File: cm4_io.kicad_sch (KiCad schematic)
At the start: 6 parts, among them CN13 1-2301994-2

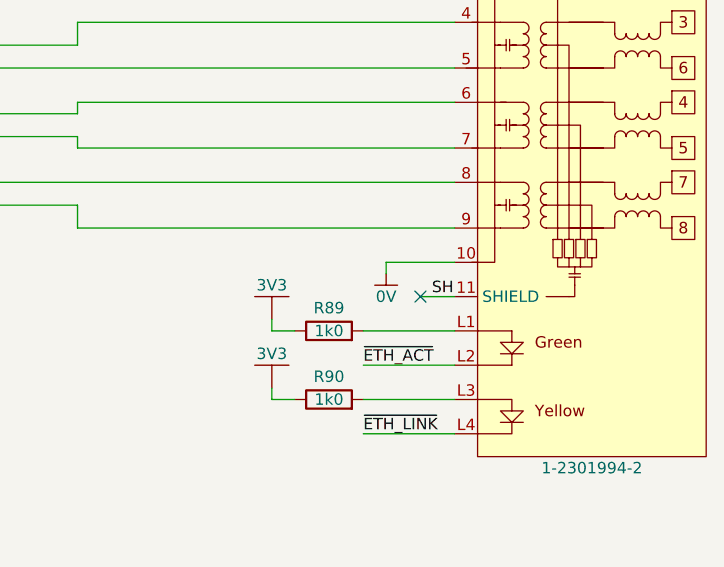
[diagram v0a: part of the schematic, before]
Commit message: Fixed connector offsets
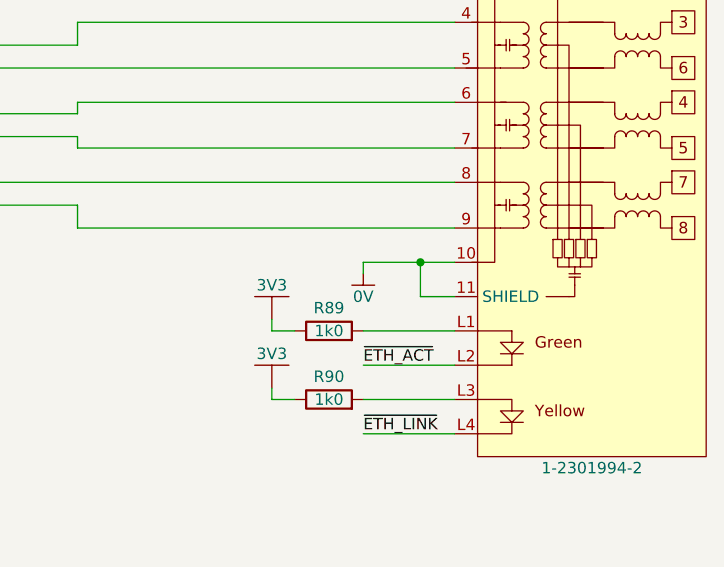
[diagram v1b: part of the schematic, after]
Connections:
- net SH is gone; now on net 0V: CN13.11 (SHIELD)
- no-connect marks 15 -> 14
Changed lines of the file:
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@@
   (junction (at 163.83 88.9) (diameter 0) (color 0 0 0 0)
+  )
+  (junction (at 264.16 78.74) (diameter 0) (color 0 0 0 0)
   )
   (junction (at 158.75 88.9) (diameter 0) (color 0 0 0 0)
@@
   (no_connect (at 83.82 57.15))
   (no_connect (at 83.82 46.99))
-  (no_connect (at 264.16 82.55))
   (no_connect (at 83.82 74.93))
   (no_connect (at 83.82 85.09))
@@
     (stroke (width 0) (type default))
   )
-  (wire (pts (xy 260.35 80.01) (xy 260.35 78.74))
-    (stroke (width 0) (type default))
-  )
   (wire (pts (xy 226.06 48.26) (xy 226.06 49.53))
     (stroke (width 0) (type default))
@@
     (stroke (width 0) (type default))
   )
-  (wire (pts (xy 260.35 78.74) (xy 267.97 78.74))
+  (wire (pts (xy 257.81 78.74) (xy 264.16 78.74))
+    (stroke (width 0) (type default))
+  )
+  (wire (pts (xy 257.81 80.01) (xy 257.81 78.74))
     (stroke (width 0) (type default))
   )
@@
     (stroke (width 0) (type default))
   )
+  (wire (pts (xy 264.16 78.74) (xy 267.97 78.74))
+    (stroke (width 0) (type default))
+  )
   (wire (pts (xy 257.81 97.79) (xy 267.97 97.79))
     (stroke (width 0) (type default))
@@
   )
   (wire (pts (xy 158.75 72.39) (xy 158.75 88.9))
+    (stroke (width 0) (type default))
+  )
+  (wire (pts (xy 264.16 78.74) (xy 264.16 82.55))
     (stroke (width 0) (type default))
   )
@@
   )
   (label "ETHC_N" (at 132.08 64.77 0) (fields_autoplaced)
-    (effects (font (size 1.27 1.27)) (justify left bottom))
-  )
-  (label "SH" (at 265.43 82.55 0) (fields_autoplaced)
     (effects (font (size 1.27 1.27)) (justify left bottom))
   )
@@
     )
   )
-  (symbol (lib_id "Power_WUT:0V") (at 260.35 80.01 0) (unit 1)
-    (in_bom no) (on_board no) (dnp no) (fields_autoplaced)
-    (property "Reference" "#PWR0215" (at 260.35 80.01 0)
-      (effects (font (size 1.27 1.27)) hide)
-    )
-    (property "Value" "0V" (at 260.35 82.55 0) (do_not_autoplace)
-      (effects (font (size 1.27 1.27)))
-    )
-    (property "Footprint" "" (at 260.35 80.01 0)
-      (effects (font (size 1.27 1.27)) hide)
-    )
-    (property "Datasheet" "" (at 260.35 80.01 0)
-      (effects (font (size 1.27 1.27)) hide)
-    )
+  (symbol (lib_id "Power_WUT:0V") (at 257.81 80.01 0) (mirror y) (unit 1)
+    (in_bom no) (on_board no) (dnp no)
+    (property "Reference" "#PWR0215" (at 257.81 80.01 0)
+      (effects (font (size 1.27 1.27)) hide)
+    )
+    (property "Value" "0V" (at 257.81 82.55 0) (do_not_autoplace)
+      (effects (font (size 1.27 1.27)))
+    )
+    (property "Footprint" "" (at 257.81 80.01 0)
+      (effects (font (size 1.27 1.27)) hide)
+    )
+    (property "Datasheet" "" (at 257.81 80.01 0)
+      (effects (font (size 1.27 1.27)) hide)
+    )
